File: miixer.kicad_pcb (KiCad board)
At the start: 2 copper layers, 100 x 100 mm, 21 parts, among them J1 USB_C_Receptacle_USB2.0_16P, SW2 SW_SPST, SW3 SW_SPST, SW4 SW_SPST, SW5 SW_SPST, SW6 SW_SPST, SW7 SW_SPST, SW8 SW_SPST, SW9 SW_SPST, U1 ESP32-C3-WROOM-02, U2 ADS1115IDGS, U3 USBLC6-2SC6

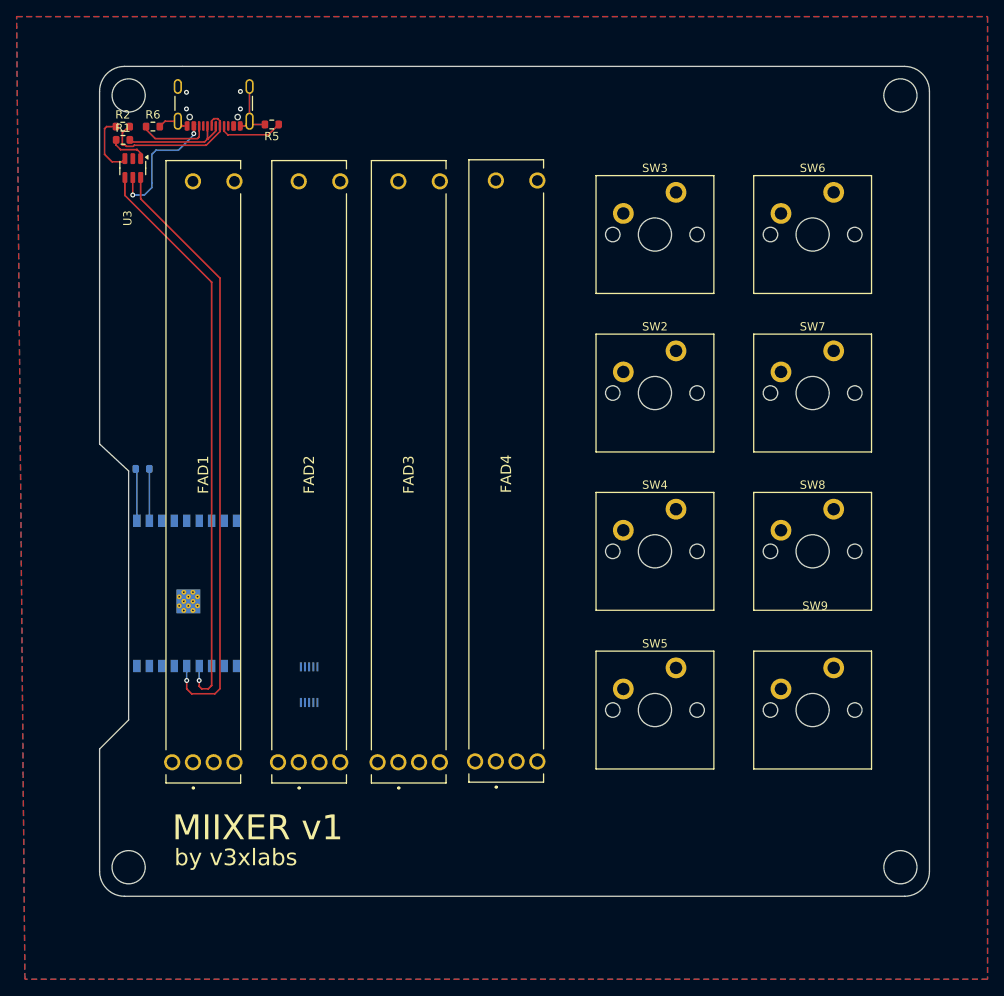
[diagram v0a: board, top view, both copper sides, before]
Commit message: Added LEDs and improved decals
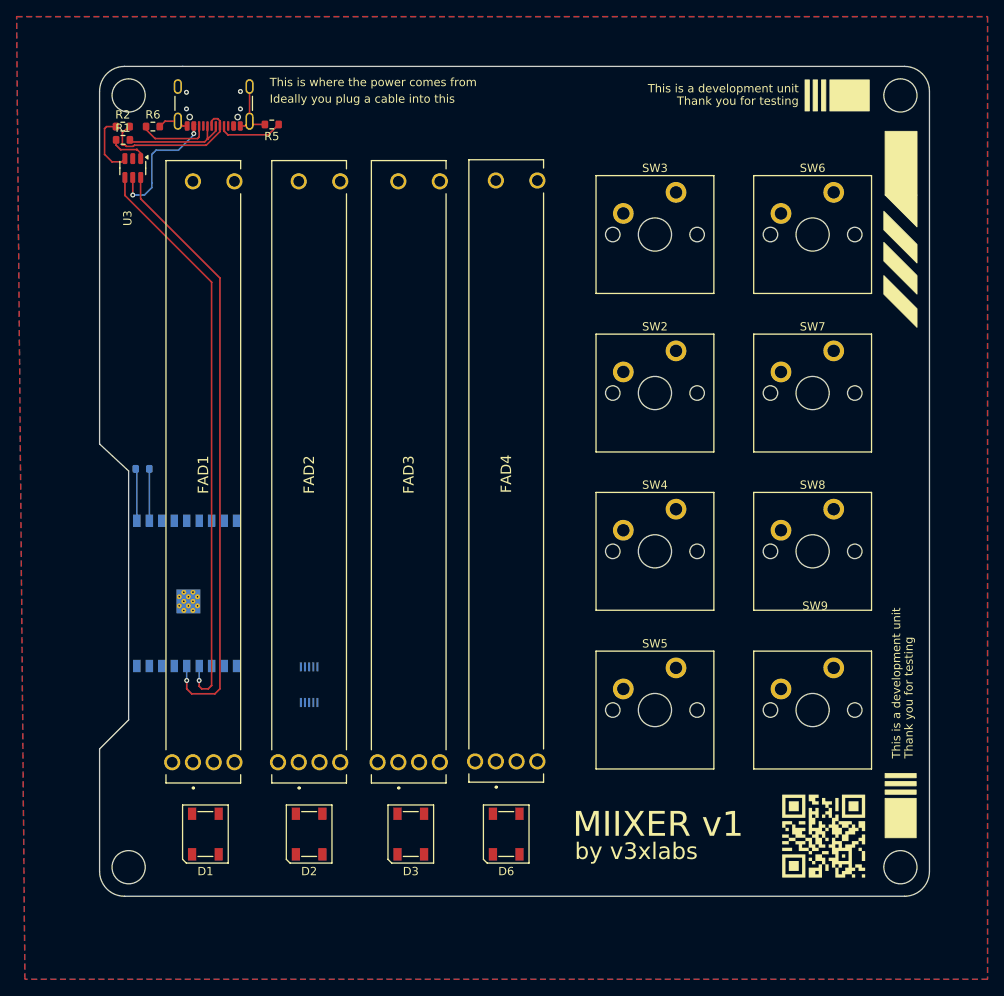
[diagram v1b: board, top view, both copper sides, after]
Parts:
- added D1: SK6812, LED_SMD:LED_SK6812_PLCC4_5.0x5.0mm_P3.2mm, F.Cu at (41.8, 119.5)
- added D2: SK6812, LED_SMD:LED_SK6812_PLCC4_5.0x5.0mm_P3.2mm, F.Cu at (54.2, 119.5)
- added D3: SK6812, LED_SMD:LED_SK6812_PLCC4_5.0x5.0mm_P3.2mm, F.Cu at (66.5, 119.5)
- added D6: SK6812, LED_SMD:LED_SK6812_PLCC4_5.0x5.0mm_P3.2mm, F.Cu at (78.0, 119.5)
- added QR*****: https://miixer.v3x.tools/_/pcb, 00_Luc:https___miixer.v3x.tools___pcb, F.Cu at (116.2, 119.8)
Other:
- board text added: "Ideally you plug a cable into this"
- board text added: "Thank you for testing"
- board text added: "This is a development unit"
- board text added: "This is where the power comes from"

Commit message: Update mcu location
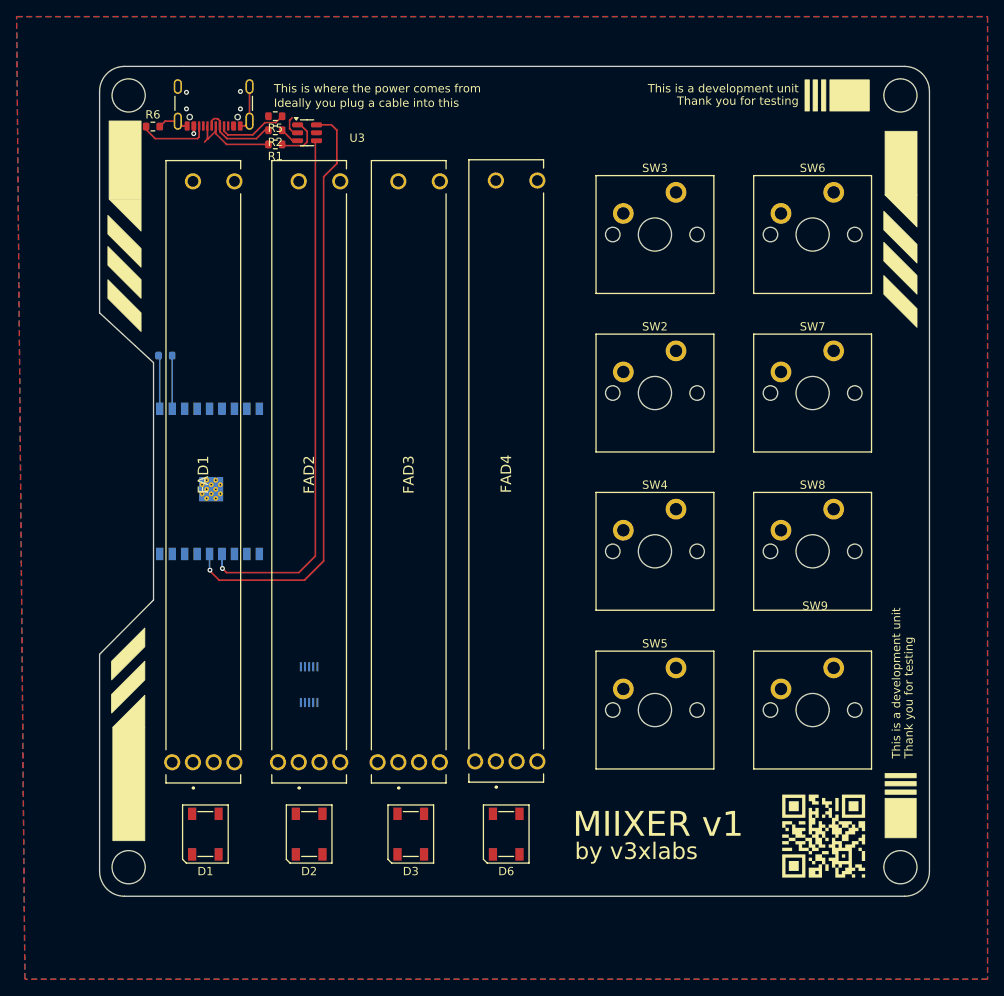
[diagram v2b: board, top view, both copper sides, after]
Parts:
- moved U3 21.4 mm to (54.0, 35.0), turned to 0 degrees
- moved R2 18.4 mm to (50.2, 34.7), turned to 180 degrees
- moved R1 18.4 mm to (50.2, 36.4), turned to 180 degrees
- moved R4 13.9 mm to (36.9, 61.9)
- moved U1 13.8 mm to (42.2, 77.0)
- moved R5 1.09 mm to (50.2, 33.0)
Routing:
- net VBUS: track 16.2 -> 1.35 mm, vias 2 -> 1
- net /USB/USB_D-_RAW: track 18.3 -> 9.73 mm
- net /MCU/USB_D-: track 69.8 -> 64.1 mm
- net /USB/USB_DN: track 7.55 -> 2.38 mm
- net /USB/USB_DP: track 4.68 -> 5.99 mm
- net /USB/USB_D+_RAW: track 13.2 -> 11.9 mm
- net GND: track 11.4 -> 12.5 mm
- net /USB/CC1: track 7.89 -> 8.73 mm
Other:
- outline, holes or cut-outs redrawn

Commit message: Update pcb
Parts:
- added QR*****: https://miixer.v3x.tools/_/pcb, 00_Luc:https___miixer.v3x.tools___pcb, B.Cu at (41.6, 119.5)
- moved U2 17.7 mm to (53.6, 83.8)
- moved R4 3.68 mm to (37.4, 65.5)
- moved QR***** 0.65 mm to (116.9, 119.7)
- turned D1 to -90 degrees
- turned D2 to -90 degrees
- turned D3 to -90 degrees
- turned D6 to -90 degrees
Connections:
- D1 pad 1: unconnected-(D1-VSS-Pad1) -> GND
- D1 pad 2: unconnected-(D1-DIN-Pad2) -> /Buttons/LED_MCU
- D1 pad 3: unconnected-(D1-VDD-Pad3) -> +3.3V
- D1 pad 4: unconnected-(D1-DOUT-Pad4) -> Net-(D1-DOUT)
- D2 pad 1: unconnected-(D2-VSS-Pad1) -> GND
- D2 pad 2: unconnected-(D2-DIN-Pad2) -> Net-(D1-DOUT)
- D2 pad 3: unconnected-(D2-VDD-Pad3) -> +3.3V
- D2 pad 4: unconnected-(D2-DOUT-Pad4) -> Net-(D2-DOUT)
- D3 pad 1: unconnected-(D3-VSS-Pad1) -> GND
- D3 pad 2: unconnected-(D3-DIN-Pad2) -> Net-(D2-DOUT)
- D3 pad 3: unconnected-(D3-VDD-Pad3) -> +3.3V
- D3 pad 4: unconnected-(D3-DOUT-Pad4) -> Net-(D3-DOUT)
- D6 pad 1: unconnected-(D6-VSS-Pad1) -> GND
- D6 pad 2: unconnected-(D6-DIN-Pad2) -> Net-(D3-DOUT)
- D6 pad 3: unconnected-(D6-VDD-Pad3) -> +3.3V
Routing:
- net +3.3V: track 6.09 -> 112.9 mm, vias 0 -> 1
- net Net-(D1-DOUT): track 0.00 -> 11.3 mm
- net Net-(D2-DOUT): track 0.00 -> 11.1 mm
- net Net-(D3-DOUT): track 0.00 -> 10.3 mm
- net /MCU/ENABLE: track 6.24 -> 2.94 mm
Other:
- board text added: "MIIXER v0.1"
- board text removed: "MIIXER v1"

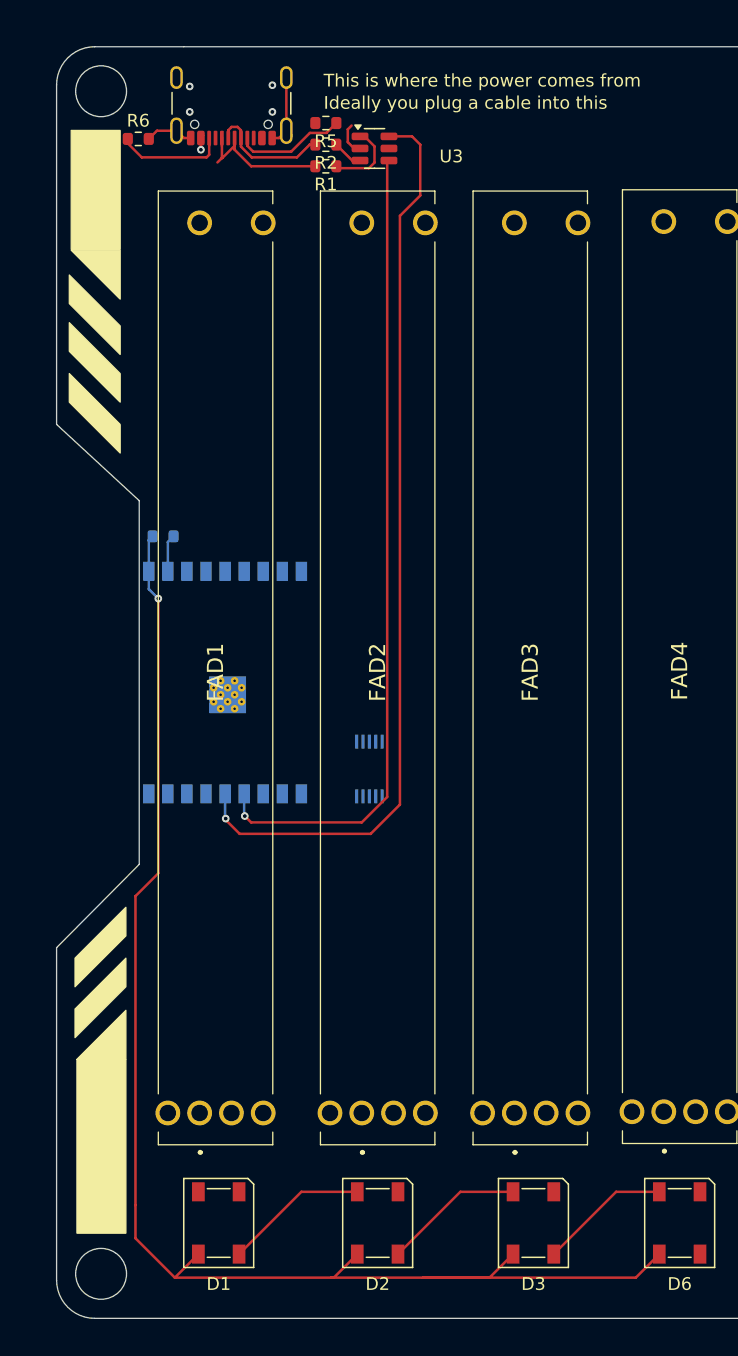
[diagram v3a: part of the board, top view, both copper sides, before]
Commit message: Update colors
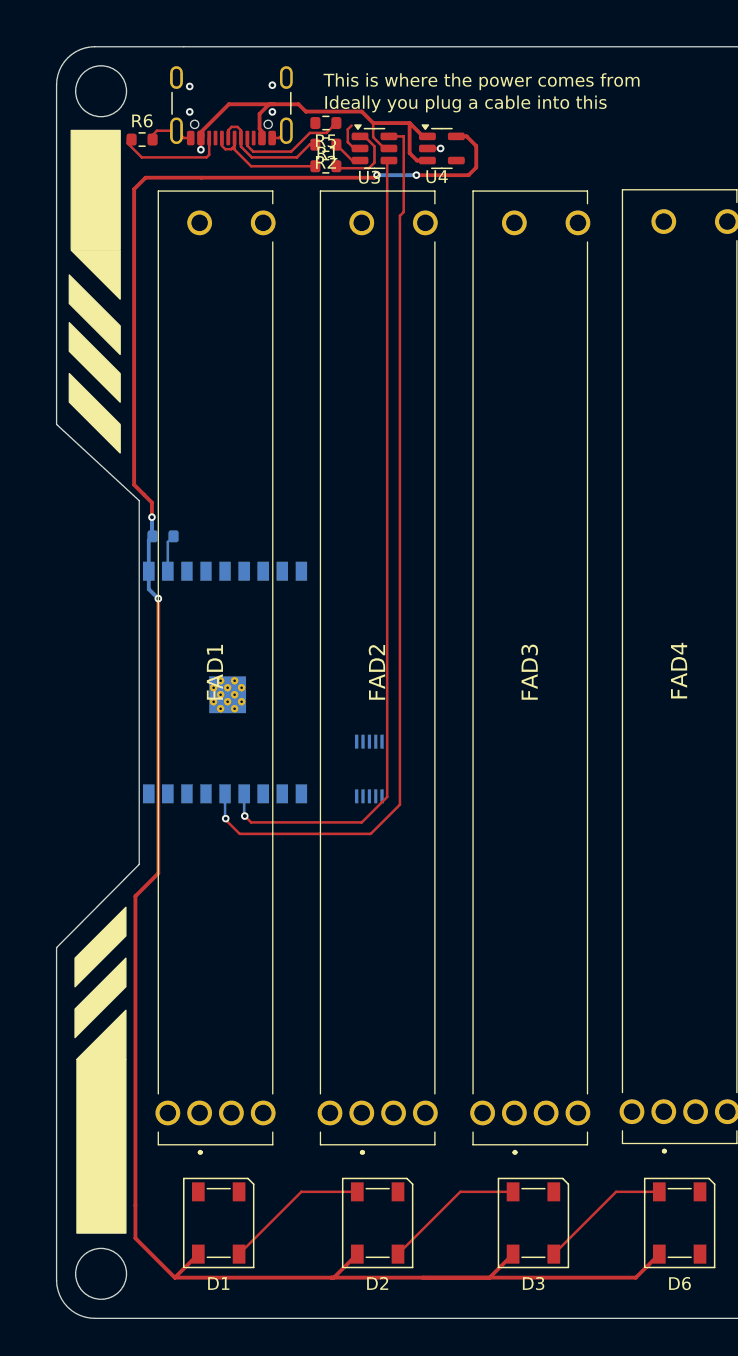
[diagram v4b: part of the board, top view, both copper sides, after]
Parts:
- added U4: AP2127K-3.3, Package_TO_SOT_SMD:SOT-23-5, F.Cu at (59.3, 35.0)
- moved R6 0.30 mm to (35.7, 34.3)
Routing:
- net +3.3V: track 112.9 -> 172.0 mm, vias 1 -> 4
- net VBUS: track 1.35 -> 31.3 mm
- net GND: track 12.5 -> 9.35 mm, vias 4 -> 5
- net /USB/USB_D+_RAW: track 11.9 -> 10.2 mm
- net /MCU/USB_D+: track 72.5 -> 71.1 mm

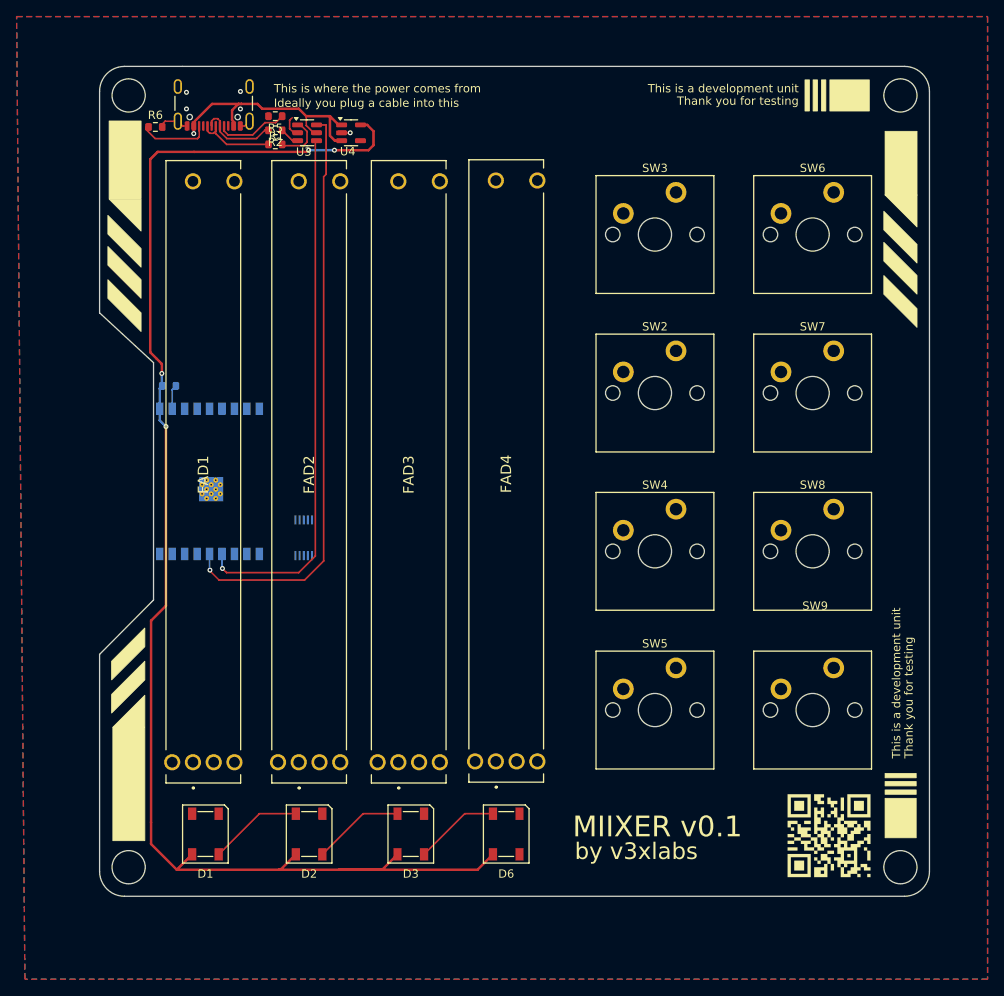
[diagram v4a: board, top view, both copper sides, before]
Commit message: Update power traces
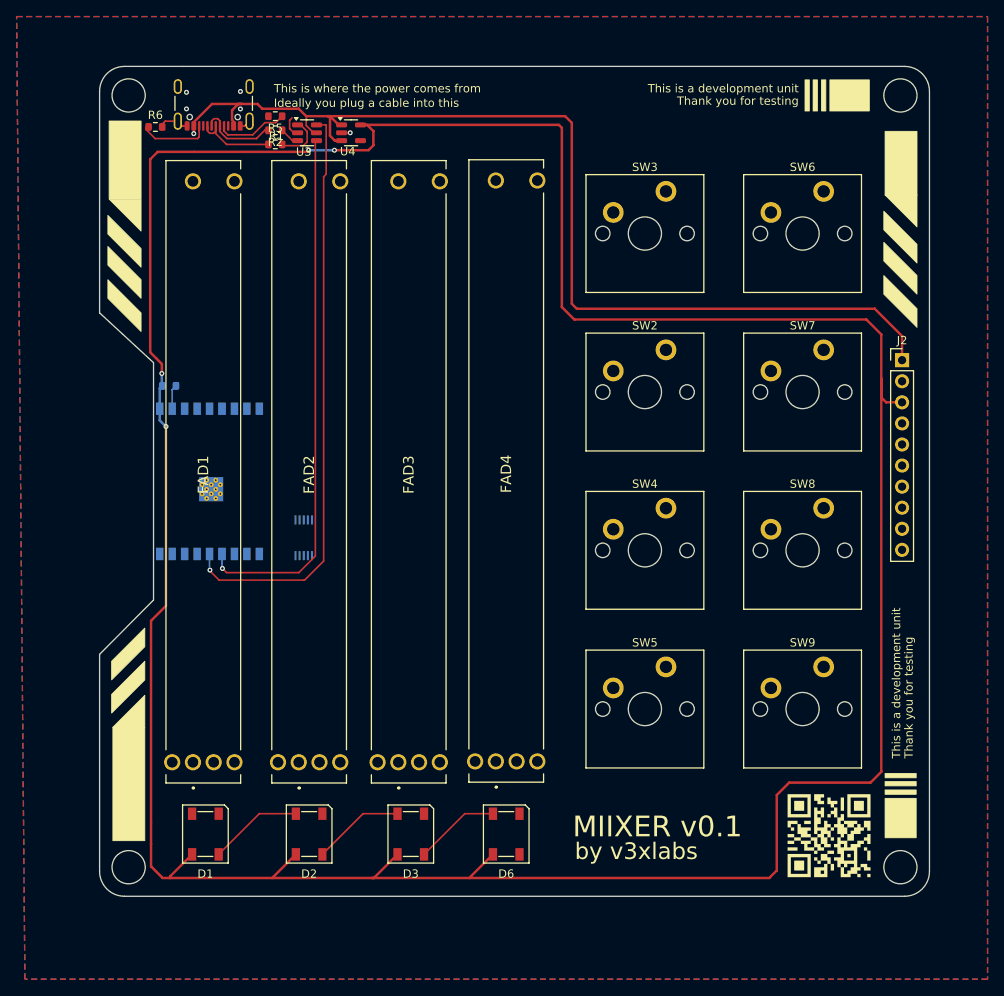
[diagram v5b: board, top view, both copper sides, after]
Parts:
- added J2: Conn_01x10_Pin, Connector_PinHeader_2.54mm:PinHeader_1x10_P2.54mm_Vertical, F.Cu at (125.7, 62.4)
- SW2, SW3, SW4, SW5, SW6, SW7, SW8, SW9: footprint PCM_Switch_Keyboard_Cherry_MX:SW_Cherry_MX_PCB_1.00u -> PCM_Switch_Keyboard_Cherry_MX:SW_Cherry_MX_PCB
- moved SW2 1.22 mm to (94.7, 66.2)
- moved SW4 1.22 mm to (94.7, 85.3)
- moved SW5 1.22 mm to (94.7, 104.4)
- moved SW7 1.22 mm to (113.7, 66.2)
- moved SW8 1.22 mm to (113.7, 85.3)
- moved SW9 1.22 mm to (113.7, 104.4)
- moved SW3 1.22 mm to (94.7, 47.1)
- moved SW6 1.22 mm to (113.7, 47.1)
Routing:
- net +3.3V: track 172.0 -> 377.3 mm
- net VBUS: track 31.3 -> 127.2 mm

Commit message: Update README
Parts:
- added U5: PCF8574T, Package_SO:SOIC-16W_7.5x10.3mm_P1.27mm, B.Cu at (57.0, 73.3)
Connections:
- J2 pad 4: unconnected-(J2-Pin_4-Pad4) -> /SDA
- J2 pad 5: unconnected-(J2-Pin_5-Pad5) -> /SCL
- SW2 pad 1: unconnected-(SW2-A-Pad1) -> Net-(SW2-A)
- SW3 pad 1: unconnected-(SW3-A-Pad1) -> Net-(SW3-A)
- SW4 pad 1: unconnected-(SW4-A-Pad1) -> Net-(SW4-A)
- SW5 pad 1: unconnected-(SW5-A-Pad1) -> Net-(SW5-A)
- SW6 pad 1: unconnected-(SW6-A-Pad1) -> Net-(SW6-A)
- SW7 pad 1: unconnected-(SW7-A-Pad1) -> Net-(SW7-A)
- SW8 pad 1: unconnected-(SW8-A-Pad1) -> Net-(SW8-A)
- SW9 pad 1: unconnected-(SW9-A-Pad1) -> Net-(SW9-A)
- U1 pad 7: unconnected-(U1-IO8-Pad7) -> /SDA
- U1 pad 8: unconnected-(U1-IO9-Pad8) -> /SCL
- U2 pad 10: unconnected-(U2-SCL-Pad10) -> /SCL
- U2 pad 3: unconnected-(U2-GND-Pad3) -> GND
- U2 pad 8: unconnected-(U2-VDD-Pad8) -> +3.3V
- U2 pad 9: unconnected-(U2-SDA-Pad9) -> /SDA
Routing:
- net /SDA: track 0.00 -> 95.9 mm, vias 0 -> 2
- net /SCL: track 0.00 -> 94.1 mm
- net +3.3V: track 377.3 -> 406.0 mm, vias 4 -> 5
